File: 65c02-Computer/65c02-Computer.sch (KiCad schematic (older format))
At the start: 7 parts, among them U1 65C02, U2 62C256, U4 28C256, X1 MXO-45HST

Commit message: Connected VIA
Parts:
- added U?: 65C22, Package_DIP:DIP-40_W15.24mm_Socket_LongPads, symbol ICs:65C22
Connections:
- net +5V: now also U?.20 (VDD)
- net A0: now also U?.38 (RS0)
- net A1: now also U?.37 (RS1)
- net A2: now also U?.36 (RS2)
- net A3: now also U?.35 (RS3)
- net D0: now also U?.33 (D0)
- net D1: now also U?.32 (D1)
- net D2: now also U?.31 (D2)
- net D3: now also U?.30 (D3)
- net D4: now also U?.29 (D4)
- net D5: now also U?.28 (D5)
- net D6: now also U?.27 (D6)
- net D7: now also U?.26 (D7)
- net GND: now also U?.1 (VSS)
- net ~WR: now also U?.22 (RWB)
- net PHI2: now reaches U1.37 (PHI2), X1.5 (OUT)
- net PHI2: now also U?.25 (PHI2)
- net Reset/~RESET renamed ~RESET
- net ~RESET: now also U?.34 (RESB)
- new net V1_CS1: U?.24 (CS1)
- new net V1_CS2B: U?.23 (CS2B)
- no-connect marks 1 -> 2
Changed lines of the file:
@@
 EESchema Schematic File Version 4
+LIBS:65c02-Computer-cache
 EELAYER 30 0
 EELAYER END
@@
 $EndComp
 $Sheet
-S 2150 4000 550  200
+S 2000 4000 550  200
 U 5DBF31D7
 F0 "Reset" 50
 F1 "reset.sch" 50
-F2 "~RESET" O R 2700 4100 50
+F2 "~RESET" O R 2550 4100 50
 $EndSheet
-Wire Wire Line
-	2700 4100 2850 4100
 Wire Wire Line
 	2850 4450 2750 4450
@@
 	4950 5150 5200 5150
 $Sheet
-S 2900 1200 1200 500
+S 2450 650  750  1000
 U 5DCD4933
 F0 "Decoding" 50
 F1 "Decoding.sch" 50
-F2 "A15" I L 2900 1350 50
-F3 "~CSROM" O R 4100 1350 50
-F4 "~CSRAM" O R 4100 1500 50
+F2 "A15" I L 2450 800 50
+F3 "~CSROM" O R 3200 750 50
+F4 "~CSRAM" O R 3200 850 50
+F5 "A14" I L 2450 900 50
+F6 "V1_CS1" O R 3200 1000 50
+F7 "A13" I L 2450 1000 50
+F8 "V1_CS2B" O R 3200 1100 50
 $EndSheet
-Text Label 2700 1350 0    50   ~ 0
+Text Label 2250 800  0    50   ~ 0
 A15
 Wire Wire Line
-	2700 1350 2900 1350
-Text Label 4500 1500 2    50   ~ 0
+	2250 800  2450 800
+Text Label 3600 850  2    50   ~ 0
 ~CSRAM
-Text Label 4500 1350 2    50   ~ 0
+Text Label 3600 750  2    50   ~ 0
 ~CSROM
 Wire Wire Line
-	4100 1350 4500 1350
-Wire Wire Line
-	4100 1500 4500 1500
+	3200 750  3600 750
+Wire Wire Line
+	3200 850  3600 850
+$Comp
+L ICs:65C22 U?
+U 1 1 5DC5464F
+P 9400 4200
+F 0 "U?" H 9400 5381 50  0000 C CNN
+F 1 "65C22" H 9400 5290 50  0000 C CNN
+F 2 "Package_DIP:DIP-40_W15.24mm_Socket_LongPads" H 9250 3850 50  0001 C CNN
+F 3 "https://www.westerndesigncenter.com/wdc/documentation/w65c22.pdf" H 9250 3850 50  0001 C CNN
+	1    9400 4200
+	1    0    0    -1
+$EndComp
+$Comp
+L power:+5V #PWR?
+U 1 1 5DC743B7
+P 8700 2850
+F 0 "#PWR?" H 8700 2700 50  0001 C CNN
+F 1 "+5V" H 8715 3023 50  0000 C CNN
+F 2 "" H 8700 2850 50  0001 C CNN
+F 3 "" H 8700 2850 50  0001 C CNN
+	1    8700 2850
+	1    0    0    -1
+$EndComp
+Wire Wire Line
+	8700 2850 8700 2900
+Wire Wire Line
+	8700 2900 8800 2900
+$Comp
+L power:GND #PWR?
+U 1 1 5DC7A360
+P 8750 5650
+F 0 "#PWR?" H 8750 5400 50  0001 C CNN
+F 1 "GND" H 8755 5477 50  0000 C CNN
+F 2 "" H 8750 5650 50  0001 C CNN
+F 3 "" H 8750 5650 50  0001 C CNN
+	1    8750 5650
+	1    0    0    -1
+$EndComp
+Wire Wire Line
+	8750 5650 8750 5600
+Wire Wire Line
+	8750 5600 8800 5600
+Wire Wire Line
+	8700 4700 8800 4700
+Text Label 8700 4700 2    50   ~ 0
+D0
+Wire Wire Line
+	8700 4800 8800 4800
+Text Label 8800 4800 2    50   ~ 0
+D1
+Wire Wire Line
+	8700 4900 8800 4900
+Text Label 8800 4900 2    50   ~ 0
+D2
+Wire Wire Line
+	8700 5000 8800 5000
+Text Label 8800 5000 2    50   ~ 0
+D3
+Wire Wire Line
+	8700 5100 8800 5100
+Text Label 8800 5100 2    50   ~ 0
+D4
+Wire Wire Line
+	8700 5200 8800 5200
+Text Label 8800 5200 2    50   ~ 0
+D5
+Wire Wire Line
+	8700 5300 8800 5300
+Text Label 8800 5300 2    50   ~ 0
+D6
+Wire Wire Line
+	8700 5400 8800 5400
+Text Label 8800 5400 2    50   ~ 0
+D7
+Entry Wire Line
+	8700 4700 8600 4800
+Entry Wire Line
+	8700 4800 8600 4900
+Entry Wire Line
+	8700 4900 8600 5000
+Entry Wire Line
+	8700 5000 8600 5100
+Entry Wire Line
+	8700 5100 8600 5200
+Entry Wire Line
+	8700 5200 8600 5300
+Entry Wire Line
+	8700 5300 8600 5400
+Entry Wire Line
+	8700 5400 8600 5500
+Wire Bus Line
+	8150 6100 8600 6100
+Connection ~ 8150 6100
+Text Label 8600 4200 0    50   ~ 0
+A0
+Text Label 8600 4300 0    50   ~ 0
+A1
+Text Label 8600 4400 0    50   ~ 0
+A2
+Text Label 8600 4500 0    50   ~ 0
+A3
+Entry Wire Line
+	8500 4300 8600 4200
+Entry Wire Line
+	8500 4400 8600 4300
+Entry Wire Line
+	8500 4500 8600 4400
+Entry Wire Line
+	8500 4600 8600 4500
+Wire Wire Line
+	8600 4200 8800 4200
+Wire Wire Line
+	8600 4300 8800 4300
+Wire Wire Line
+	8600 4400 8800 4400
+Wire Wire Line
+	8600 4500 8800 4500
+Wire Bus Line
+	6950 6000 8500 6000
+Connection ~ 6950 6000
+Text GLabel 8700 4000 0    50   Input ~ 0
+~WR
+Wire Wire Line
+	8700 4000 8800 4000
+Text Label 2650 4100 0    50   ~ 0
+~RESET
+Wire Wire Line
+	2550 4100 2850 4100
+Text Label 1900 3750 0    50   ~ 0
+PHI2
+Text Label 8500 3500 0    50   ~ 0
+~RESET
+Wire Wire Line
+	8500 3500 8800 3500
+Wire Wire Line
+	8800 3100 8500 3100
+Text Label 8500 3100 0    50   ~ 0
+PHI2
+Wire Wire Line
+	8800 3800 8400 3800
+Text Label 8400 3800 0    50   ~ 0
+V1_CS2B
+Wire Wire Line
+	8800 3700 8400 3700
+Text Label 8400 3700 0    50   ~ 0
+V1_CS1
+Wire Wire Line
+	3200 1000 3600 1000
+Wire Wire Line
+	3200 1100 3600 1100
+Wire Wire Line
+	2450 900  2250 900
+Wire Wire Line
+	2450 1000 2250 1000
+Text Label 2250 900  0    50   ~ 0
+A14
+Text Label 2250 1000 0    50   ~ 0
+A13
+Text Label 3600 1000 2    50   ~ 0
+V1_CS1
+Text Label 3600 1100 2    50   ~ 0
+V1_CS2B
+NoConn ~ 8800 3300
+Wire Bus Line
+	8500 4300 8500 6000
 Wire Bus Line
 	8150 3350 8150 6100
@@
 	2650 4550 2650 6100
 Wire Bus Line
+	8600 4800 8600 6100
+Wire Bus Line
 	5350 3350 5350 6000

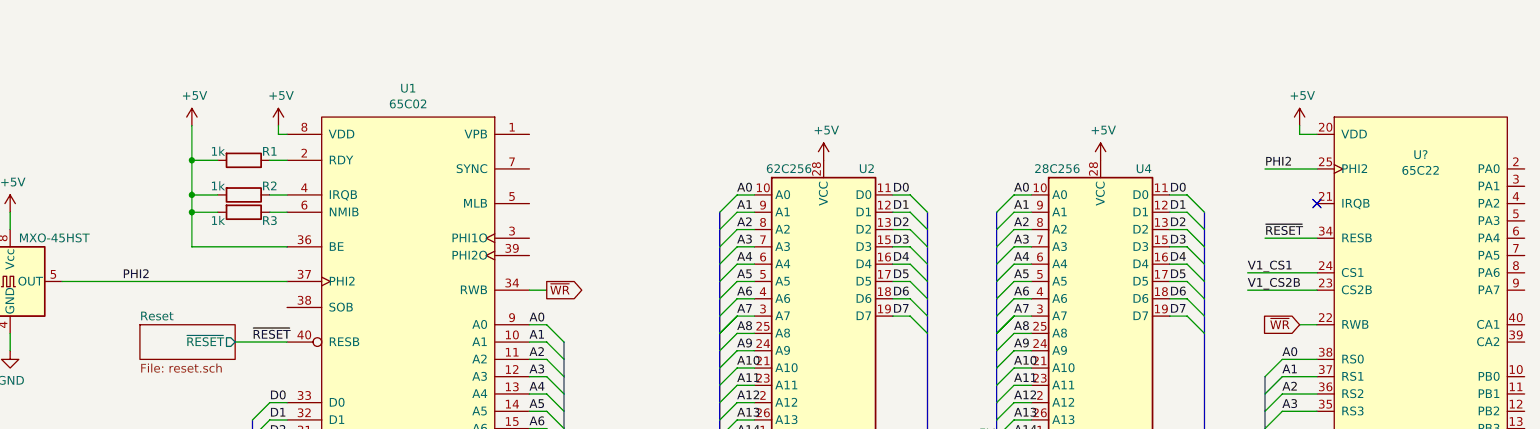
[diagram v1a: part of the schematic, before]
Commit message: Rename clock signals and add annotations
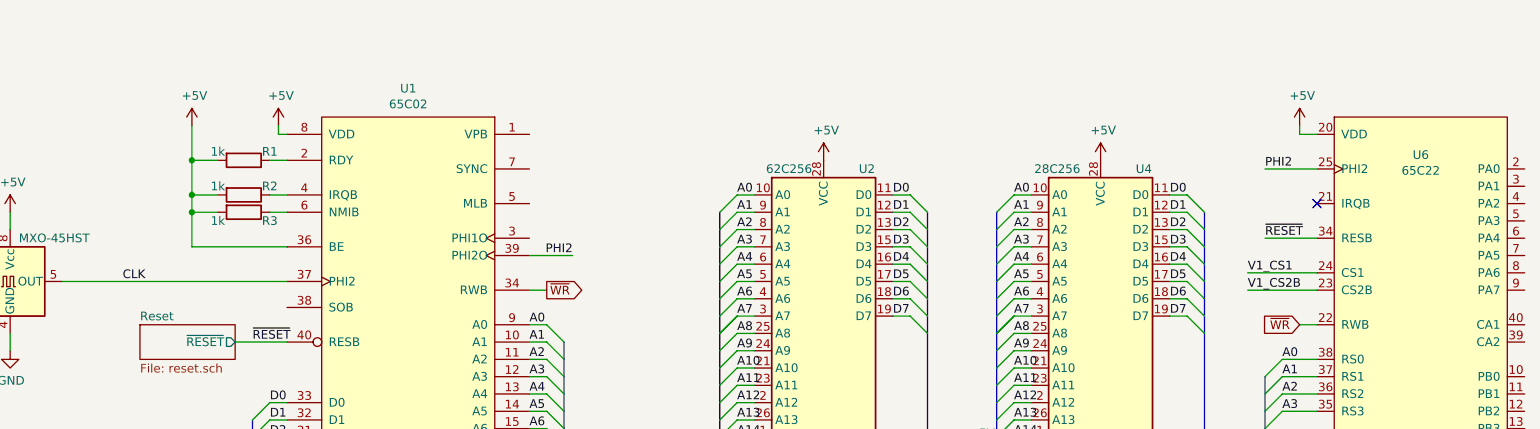
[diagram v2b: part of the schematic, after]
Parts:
- gave numbers to parts that had none: 1
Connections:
- net PHI2: now also U1.39 (PHI2O); no longer U1.37 (PHI2), X1.5 (OUT)
- new net CLK: U1.37 (PHI2), X1.5 (OUT)
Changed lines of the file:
@@
 	3200 850  3600 850
 $Comp
-L ICs:65C22 U?
+L ICs:65C22 U6
 U 1 1 5DC5464F
 P 9400 4200
-F 0 "U?" H 9400 5381 50  0000 C CNN
+F 0 "U6" H 9400 5381 50  0000 C CNN
 F 1 "65C22" H 9400 5290 50  0000 C CNN
 F 2 "Package_DIP:DIP-40_W15.24mm_Socket_LongPads" H 9250 3850 50  0001 C CNN
@@
 $EndComp
 $Comp
-L power:+5V #PWR?
+L power:+5V #PWR019
 U 1 1 5DC743B7
 P 8700 2850
-F 0 "#PWR?" H 8700 2700 50  0001 C CNN
+F 0 "#PWR019" H 8700 2700 50  0001 C CNN
 F 1 "+5V" H 8715 3023 50  0000 C CNN
 F 2 "" H 8700 2850 50  0001 C CNN
@@
 	8700 2900 8800 2900
 $Comp
-L power:GND #PWR?
+L power:GND #PWR020
 U 1 1 5DC7A360
 P 8750 5650
-F 0 "#PWR?" H 8750 5400 50  0001 C CNN
+F 0 "#PWR020" H 8750 5400 50  0001 C CNN
 F 1 "GND" H 8755 5477 50  0000 C CNN
 F 2 "" H 8750 5650 50  0001 C CNN
@@
 Wire Wire Line
 	2550 4100 2850 4100
-Text Label 1900 3750 0    50   ~ 0
-PHI2
 Text Label 8500 3500 0    50   ~ 0
 ~RESET
@@
 Wire Wire Line
 	8800 3100 8500 3100
-Text Label 8500 3100 0    50   ~ 0
-PHI2
 Wire Wire Line
 	8800 3800 8400 3800
@@
 V1_CS2B
 NoConn ~ 8800 3300
+Text Label 8500 3100 0    50   ~ 0
+PHI2
+Text Label 1900 3750 0    50   ~ 0
+CLK
+Wire Wire Line
+	4250 3600 4500 3600
 Wire Bus Line
 	8500 4300 8500 6000
+Wire Bus Line
+	8600 4800 8600 6100
 Wire Bus Line
 	8150 3350 8150 6100
@@
 	2650 4550 2650 6100
 Wire Bus Line
-	8600 4800 8600 6100
-Wire Bus Line
 	5350 3350 5350 6000
 Wire Bus Line
@@
 Wire Bus Line
 	4450 4100 4450 6000
+Text Label 4500 3600 2    50   ~ 0
+PHI2
 $EndSCHEMATC

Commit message: Add firmware and utilities
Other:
- moved on the sheet: R1, R2, R3, U1, U2, U4, U6, X1

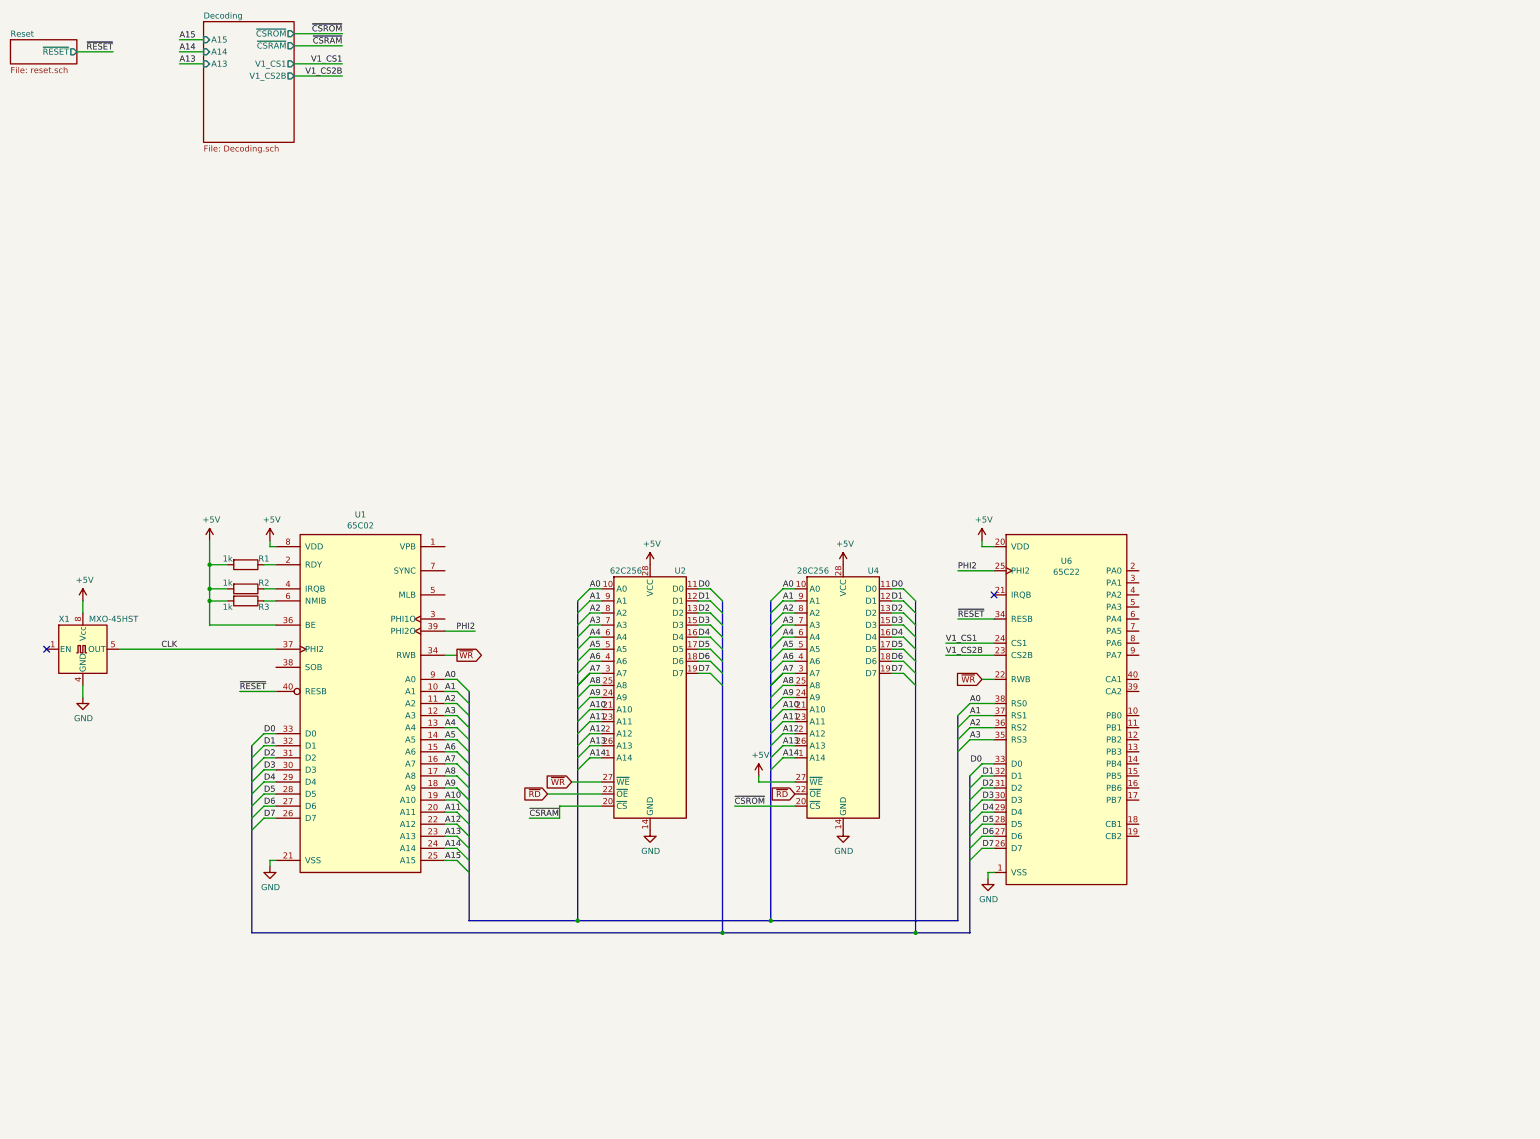
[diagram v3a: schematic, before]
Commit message: Update pcb and put arduino sketch
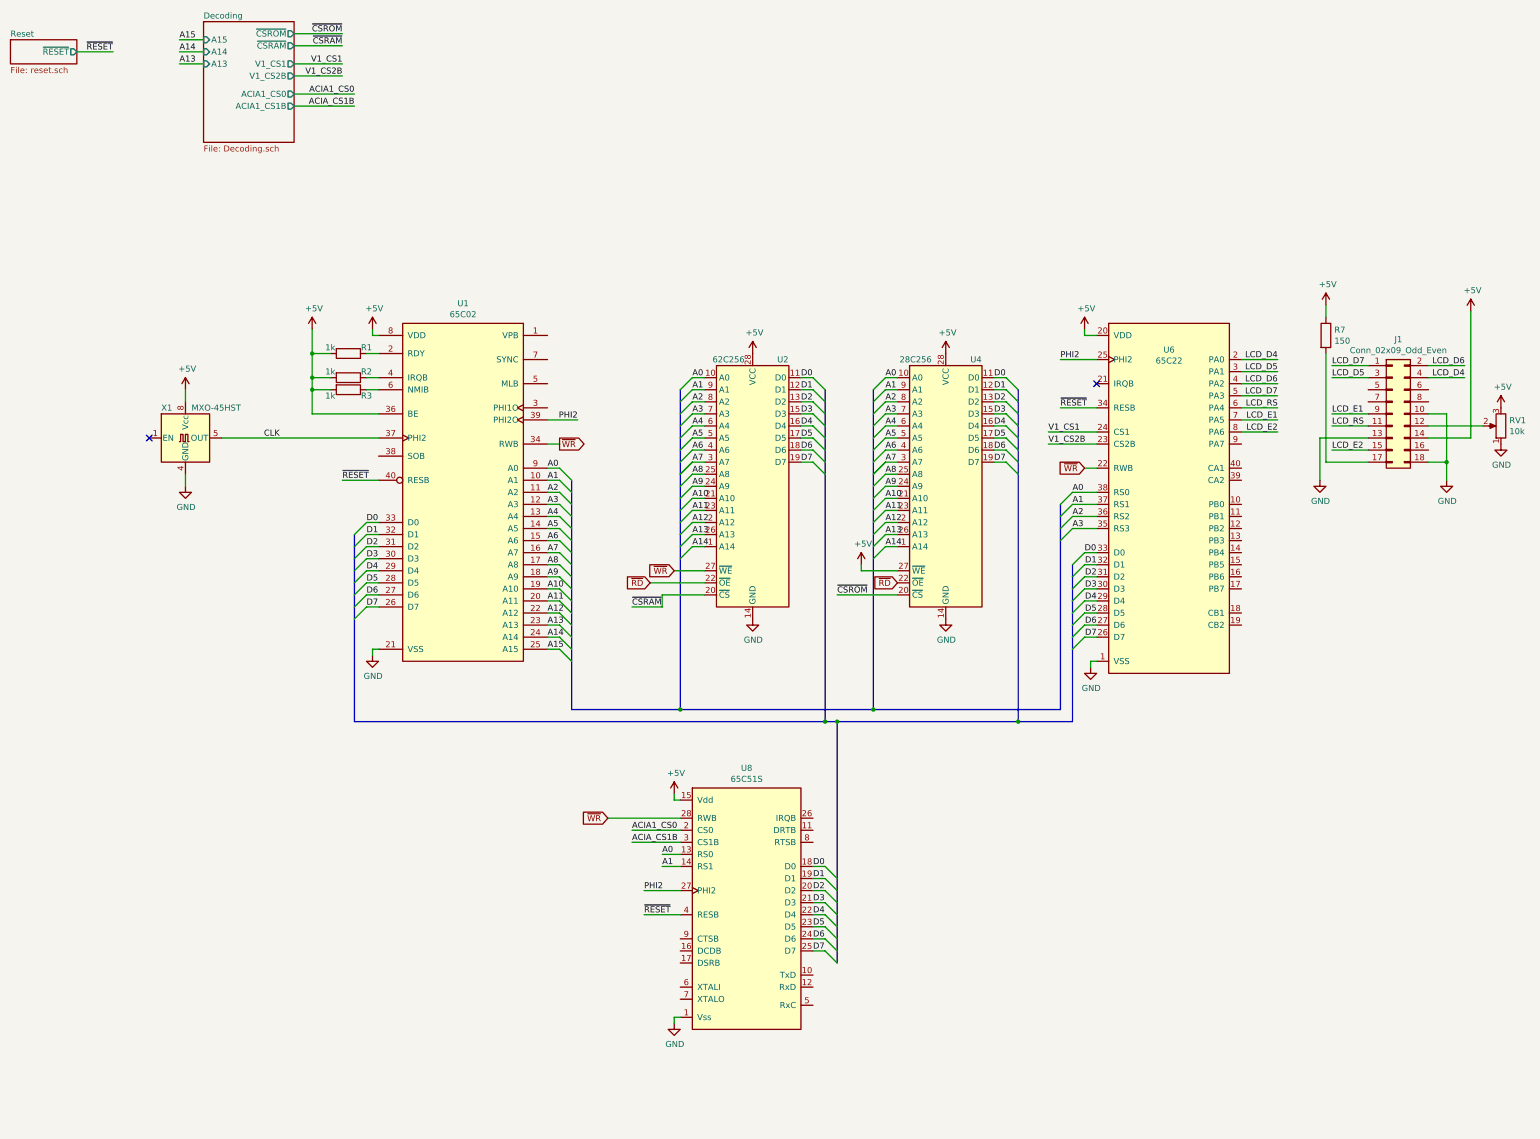
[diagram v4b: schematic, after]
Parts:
- added J1: Conn_02x09_Odd_Even, Connector_PinHeader_2.54mm:PinHeader_2x09_P2.54mm_Vertical, symbol Connector_Generic:Conn_02x09_Odd_Even
- added R7: 150, Resistor_SMD:R_0603_1608Metric, symbol device:R
- added RV1: 10k, Connector_PinHeader_2.54mm:PinHeader_1x03_P2.54mm_Vertical, symbol device:R_POT
- added U8: 65C51S, Package_DIP:DIP-28_W15.24mm_Socket_LongPads, symbol ICs:65C51S
- U1: footprint Package_DIP:DIP-40_W15.24mm_Socket -> Package_DIP:DIP-40_W15.24mm_Socket_LongPads
- U2, U4: footprint Package_DIP:DIP-28_W15.24mm_Socket -> Package_DIP:DIP-28_W15.24mm_Socket_LongPads
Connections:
- net +5V: now also J1.14 (Pin_14), R7.1, RV1.3, U8.15 (Vdd)
- net A0: now also U8.13 (RS0)
- net A1: now also U8.14 (RS1)
- net D0: now also U8.18 (D0)
- net D1: now also U8.19 (D1)
- net D2: now also U8.20 (D2)
- net D3: now also U8.21 (D3)
- net D4: now also U8.22 (D4)
- net D5: now also U8.23 (D5)
- net D6: now also U8.24 (D6)
- net D7: now also U8.25 (D7)
- net GND: now also J1.10 (Pin_10), J1.13 (Pin_13), J1.18 (Pin_18), RV1.1, U8.1 (Vss)
- net PHI2: now also U8.27 (PHI2)
- net ~RESET: now also U8.4 (RESB)
- net ~WR: now also U8.28 (RWB)
- net LCD_D4: now reaches U6.2 (PA0)
- net LCD_D4: now also J1.4 (Pin_4)
- net LCD_D5: now reaches U6.3 (PA1)
- net LCD_D5: now also J1.3 (Pin_3)
- net LCD_D6: now reaches U6.4 (PA2)
- net LCD_D6: now also J1.2 (Pin_2)
- net LCD_D7: now reaches U6.5 (PA3)
- net LCD_D7: now also J1.1 (Pin_1)
- net LCD_RS: now reaches U6.6 (PA4)
- net LCD_RS: now also J1.11 (Pin_11)
- net LCD_E1: now reaches U6.7 (PA5)
- net LCD_E1: now also J1.9 (Pin_9)
- net LCD_E2: now reaches U6.8 (PA6)
- net LCD_E2: now also J1.15 (Pin_15)
- new net: J1.12 (Pin_12), RV1.2
- new net: J1.17 (Pin_17), R7.2
- new net ACIA1_CS0: U8.2 (CS0)
- new net ACIA_CS1B: U8.3 (CS1B)
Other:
- moved on the sheet: R1, R2, R3, U1, U2, U4, U6, X1

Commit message: Create v2
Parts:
- added C1: 27p, Capacitor_THT:C_Disc_D3.8mm_W2.6mm_P2.50mm, symbol device:C
- added J1: Barrel_Jack, Connector_BarrelJack:BarrelJack_CUI_PJ-102AH_Horizontal, symbol Connector:Barrel_Jack
- added J2: Conn_01x06, Connector_PinSocket_2.54mm:PinSocket_1x06_P2.54mm_Horizontal, symbol Connector_Generic:Conn_01x06
- added U6: 65C22, Package_DIP:DIP-40_W15.24mm_Socket_LongPads, symbol ICs:65C22
- added Y1: 1.8432MHz, Crystal:Crystal_HC49-U_Vertical, symbol device:Crystal
- R1, R2, R3: footprint Resistor_SMD:R_0603_1608Metric -> Resistor_THT:R_Axial_DIN0207_L6.3mm_D2.5mm_P10.16mm_Horizontal
- R4: renamed from R7; footprint Resistor_SMD:R_0603_1608Metric -> Resistor_THT:R_Axial_DIN0207_L6.3mm_D2.5mm_P10.16mm_Horizontal
- renumbered J1 to J3, U8 to U2, U2 to U3, U6 to U5
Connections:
- net ACIA1_CS0 is gone; now on net +5V: U2.2 (CS0)
- net V1_CS1 is gone; now on net +5V: U5.24 (CS1)
- net +5V: now also J1.1, U6.20 (VDD), U6.24 (CS1)
- net A0: now also U6.38 (RS0)
- net A1: now also U6.37 (RS1)
- net A2: now also U6.36 (RS2)
- net A3: now also U6.35 (RS3)
- net D0: now also U6.33 (D0)
- net D1: now also U6.32 (D1)
- net D2: now also U6.31 (D2)
- net D3: now also U6.30 (D3)
- net D4: now also U6.29 (D4)
- net D5: now also U6.28 (D5)
- net D6: now also U6.27 (D6)
- net D7: now also U6.26 (D7)
- net GND: now also U2.16 (DCDB), U2.17 (DSRB), U2.9 (CTSB), C1.2, J1.2, J2.6 (Pin_6), U6.1 (VSS)
- net PHI2: now also U6.25 (PHI2)
- net ~RESET: now also U6.34 (RESB)
- net ~WR: now also U6.22 (RWB)
- net at U2.10 (TxD): now also J2.2 (Pin_2)
- net at U2.12 (RxD): now also J2.3 (Pin_3)
- net at U2.6 (XTALI): now also Y1.2
- net at U2.7 (XTALO): now also C1.1, Y1.1
- new net V2_CS2B: U6.23 (CS2B)
- no-connect marks 2 -> 3
